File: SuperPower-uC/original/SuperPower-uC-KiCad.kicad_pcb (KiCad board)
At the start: 4 copper layers, 92.2 x 45.2 mm, 149 parts, among them J1 JST_PH_S2B_thru, J10 Conn_01x13_Male, J3 Conn_01x02_Male, J4 DNP/JST_ZH_S2B_thru, J5 DNP/JST_XH_S2B_thru, J6 Conn_01x02_Male, J7 Conn_01x14_Male, J8 Conn_01x14_Male, J9 Conn_01x13_Female, Q1 DMN2019UTS, Q10 2N7002A, Q11 2N7002A, Q12 DMP2035UVT, Q13 DMP2035UVT, Q14 DMP2035UVT, Q15 DMN3023L, Q2 Si3421DV, Q3 DMN3023L, Q4 2N7002A, Q5 DMP2035UVT, Q6 BSS84-7-F, Q7 S8050, Q8 S8050, Q9 2N7002A, SW1 DNP/SKRKAEE020, U1 AP9101CK6-AYTRG1, U10 TPS63070RNMT, U2 USB-C, U3 IP4220CZ6, U4 LTC4162EUFD-LAD, U5 RV-3028-C7, U6 CP2102N-A01-GQFN28, U7 ESP32-WROOM32, U8 TPS70933DRVT, U9 TPS63070RNMT

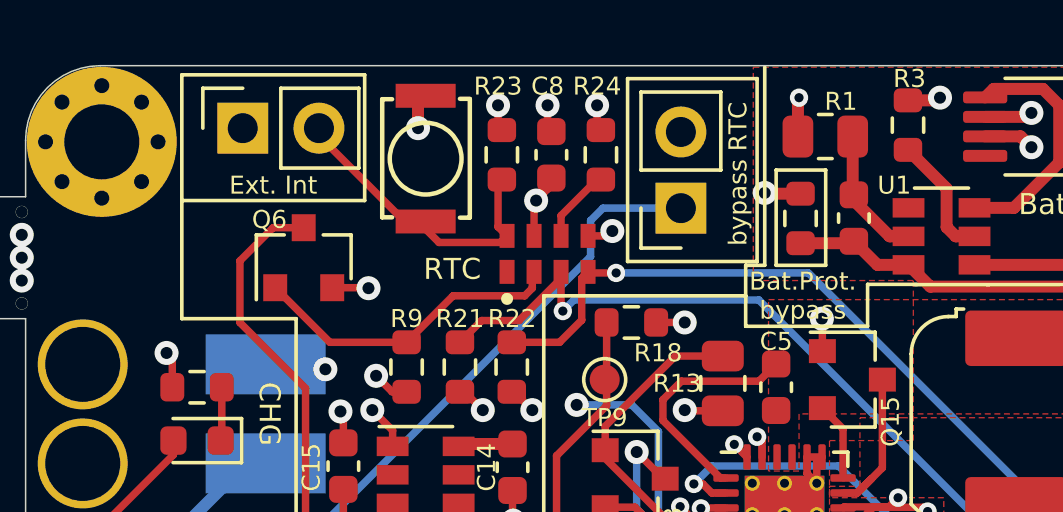
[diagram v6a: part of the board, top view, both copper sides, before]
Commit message: turned RTC bypass connector 90°
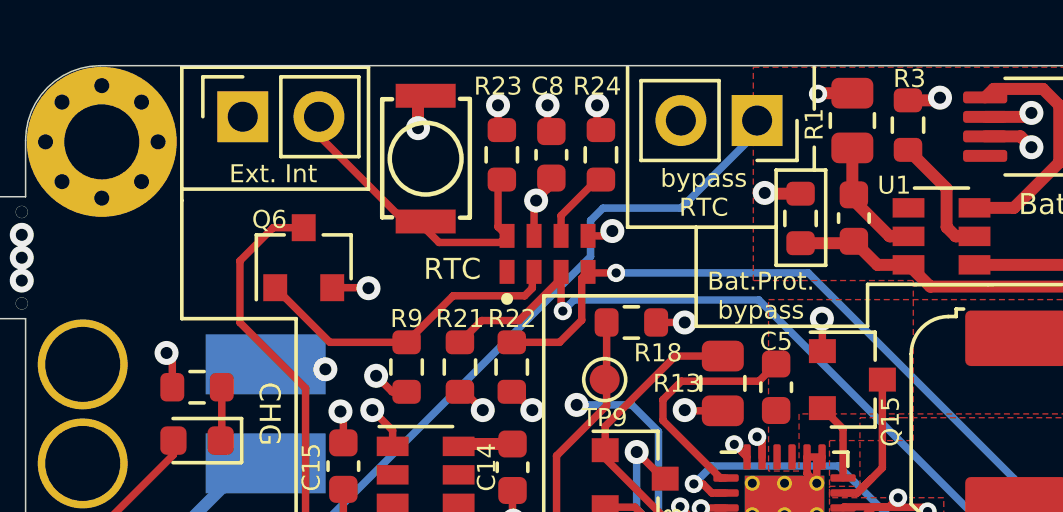
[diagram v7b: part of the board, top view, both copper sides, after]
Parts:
- moved JP2 3.87 mm to (173.1, 78.2), turned to 270 degrees
- moved R1 1.05 mm to (176.3, 78.2), turned to 270 degrees
- moved J6 0.38 mm to (156.0, 78.1)
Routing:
- net Net-(JP2-Pad1): track 27.6 -> 31.5 mm

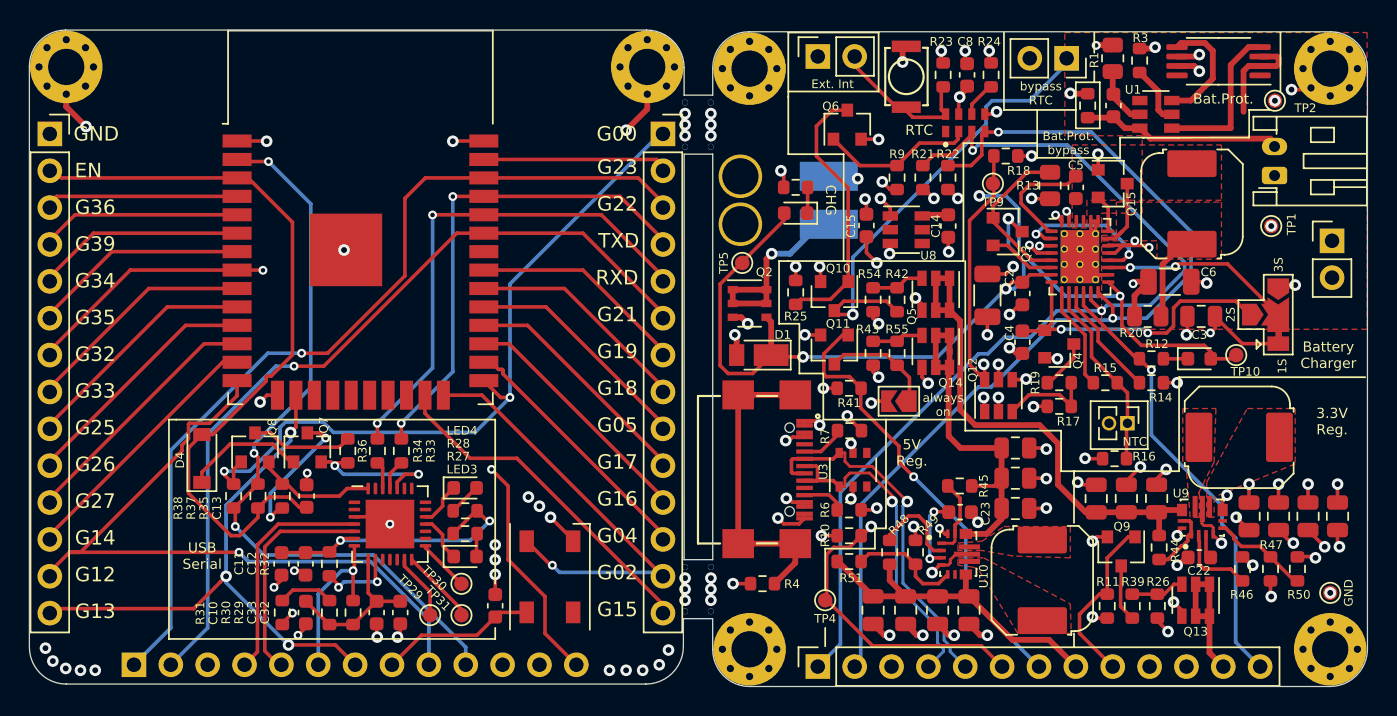
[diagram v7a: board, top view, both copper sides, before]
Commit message: Add connector for 3v3 and 5v out
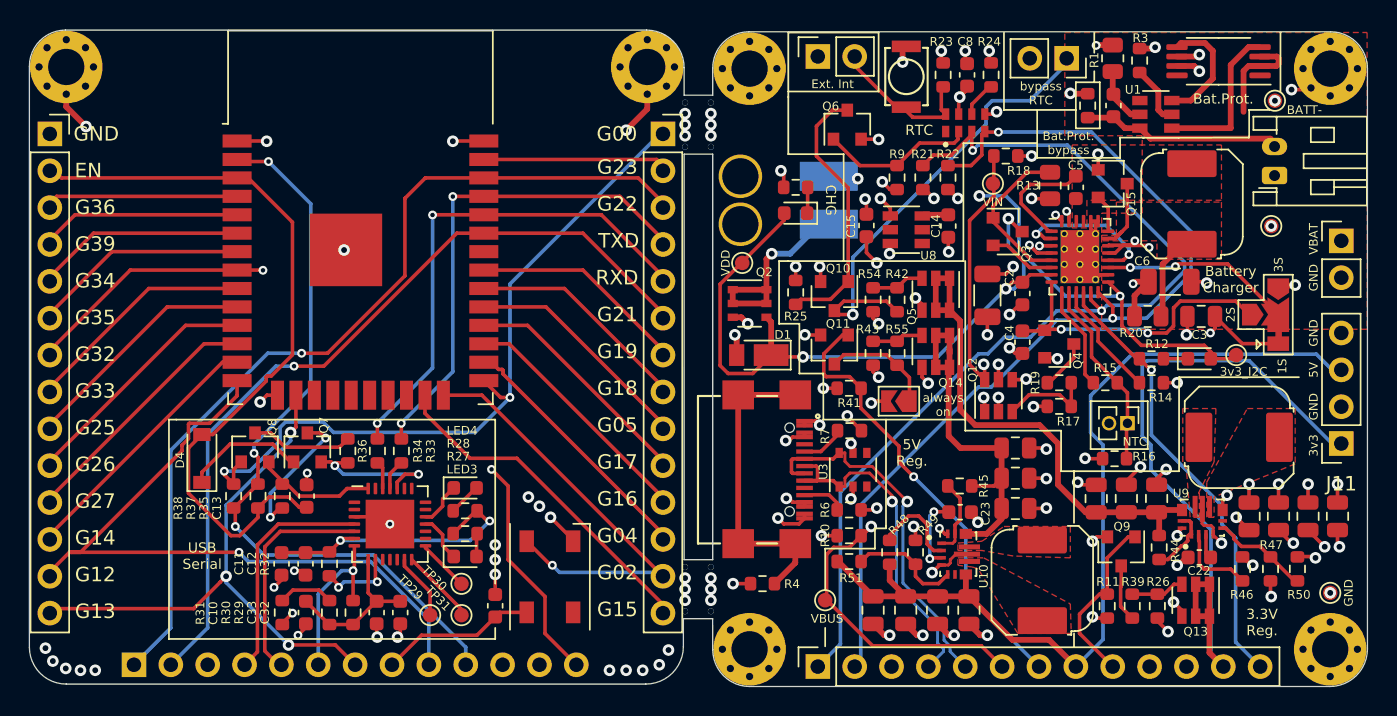
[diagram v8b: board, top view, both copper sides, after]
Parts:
- added J11: Conn_01x04_Male, Connector_PinSocket_2.54mm:PinSocket_1x04_P2.54mm_Vertical, F.Cu at (192.0, 104.8)
- moved J5 0.63 mm to (192.0, 90.8)
- renumbered GND to TP3
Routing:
- net /3v3: track 10.2 -> 48.8 mm
- net /5V: track 23.9 -> 61.9 mm
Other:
- board text added: "3v3"
- board text added: "3v3_I2C"
- board text added: "5V"
- board text added: "BATT-"
- board text added: "VBAT"
- board text added: "VDD"
